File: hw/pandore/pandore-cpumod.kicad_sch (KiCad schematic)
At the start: 11 parts, among them U1 LattePanda_Mu

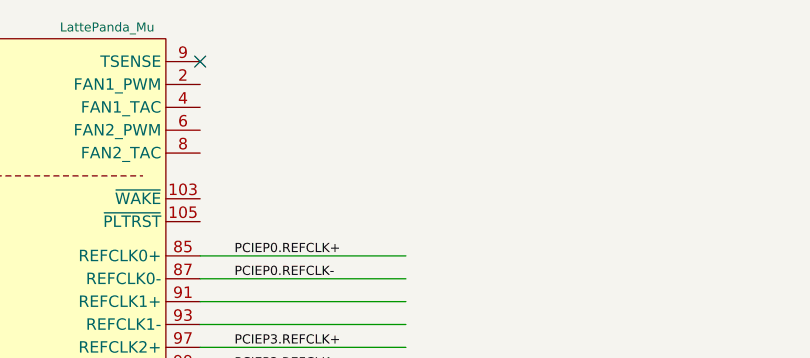
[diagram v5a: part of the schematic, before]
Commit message: lcd control circuit added fan interface added rgba output pinout for management mcu accessories done
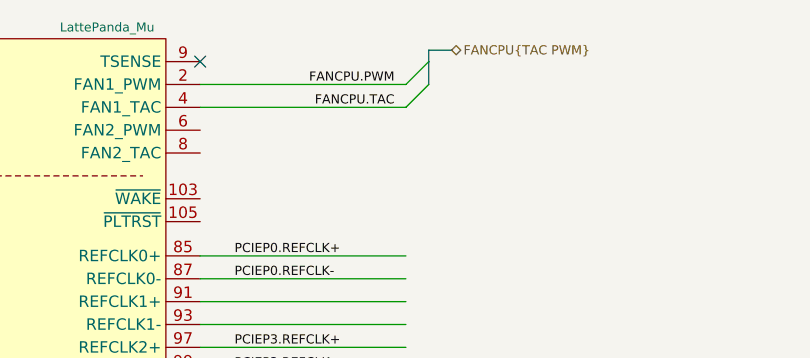
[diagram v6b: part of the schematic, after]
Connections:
- net FANCPU.PWM: now reaches U1.2 (FAN1_PWM)
- net FANCPU.TAC: now reaches U1.4 (FAN1_TAC)
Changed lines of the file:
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@@
 	)
 	(bus_entry
+		(at 246.38 21.59)
+		(size -2.54 2.54)
+		(stroke
+			(width 0)
+			(type default)
+		)
+	)
+	(bus_entry
 		(at 104.14 111.76)
 		(size -2.54 2.54)
@@
 	)
 	(bus_entry
+		(at 246.38 19.05)
+		(size -2.54 2.54)
+		(stroke
+			(width 0)
+			(type default)
+		)
+	)
+	(bus_entry
 		(at 256.54 204.47)
 		(size -2.54 2.54)
@@
 	(wire
 		(pts
+			(xy 220.98 21.59) (xy 243.84 21.59)
+		)
+		(stroke
+			(width 0)
+			(type default)
+		)
+	)
+	(wire
+		(pts
 			(xy 276.86 162.56) (xy 275.59 162.56)
 		)
@@
 		)
 	)
+	(bus
+		(pts
+			(xy 248.92 17.78) (xy 246.38 17.78)
+		)
+		(stroke
+			(width 0)
+			(type default)
+		)
+	)
 	(wire
 		(pts
@@
 	(bus
 		(pts
+			(xy 246.38 19.05) (xy 246.38 21.59)
+		)
+		(stroke
+			(width 0)
+			(type default)
+		)
+	)
+	(bus
+		(pts
 			(xy 104.14 114.3) (xy 104.14 115.57)
 		)
@@
 	(bus
 		(pts
+			(xy 246.38 17.78) (xy 246.38 19.05)
+		)
+		(stroke
+			(width 0)
+			(type default)
+		)
+	)
+	(bus
+		(pts
 			(xy 104.14 95.25) (xy 104.14 97.79)
 		)
@@
 	(wire
 		(pts
+			(xy 220.98 24.13) (xy 243.84 24.13)
+		)
+		(stroke
+			(width 0)
+			(type default)
+		)
+	)
+	(wire
+		(pts
 			(xy 106.68 52.07) (xy 137.16 52.07)
 		)
@@
 		)
 	)
+	(label "FANCPU.TAC"
+		(at 242.57 24.13 180)
+		(effects
+			(font
+				(size 1.016 1.016)
+			)
+			(justify right bottom)
+		)
+	)
 	(label "USBP7.D-"
 		(at 134.62 156.21 180)
@@
 		)
 	)
+	(label "FANCPU.PWM"
+		(at 242.57 21.59 180)
+		(effects
+			(font
+				(size 1.016 1.016)
+			)
+			(justify right bottom)
+		)
+	)
 	(label "USBP3.D-"
 		(at 134.62 146.05 180)
@@
 		)
 	)
+	(hierarchical_label "FANCPU{TAC PWM}"
+		(shape bidirectional)
+		(at 248.92 17.78 0)
+		(effects
+			(font
+				(size 1.016 1.016)
+			)
+			(justify left)
+		)
+	)

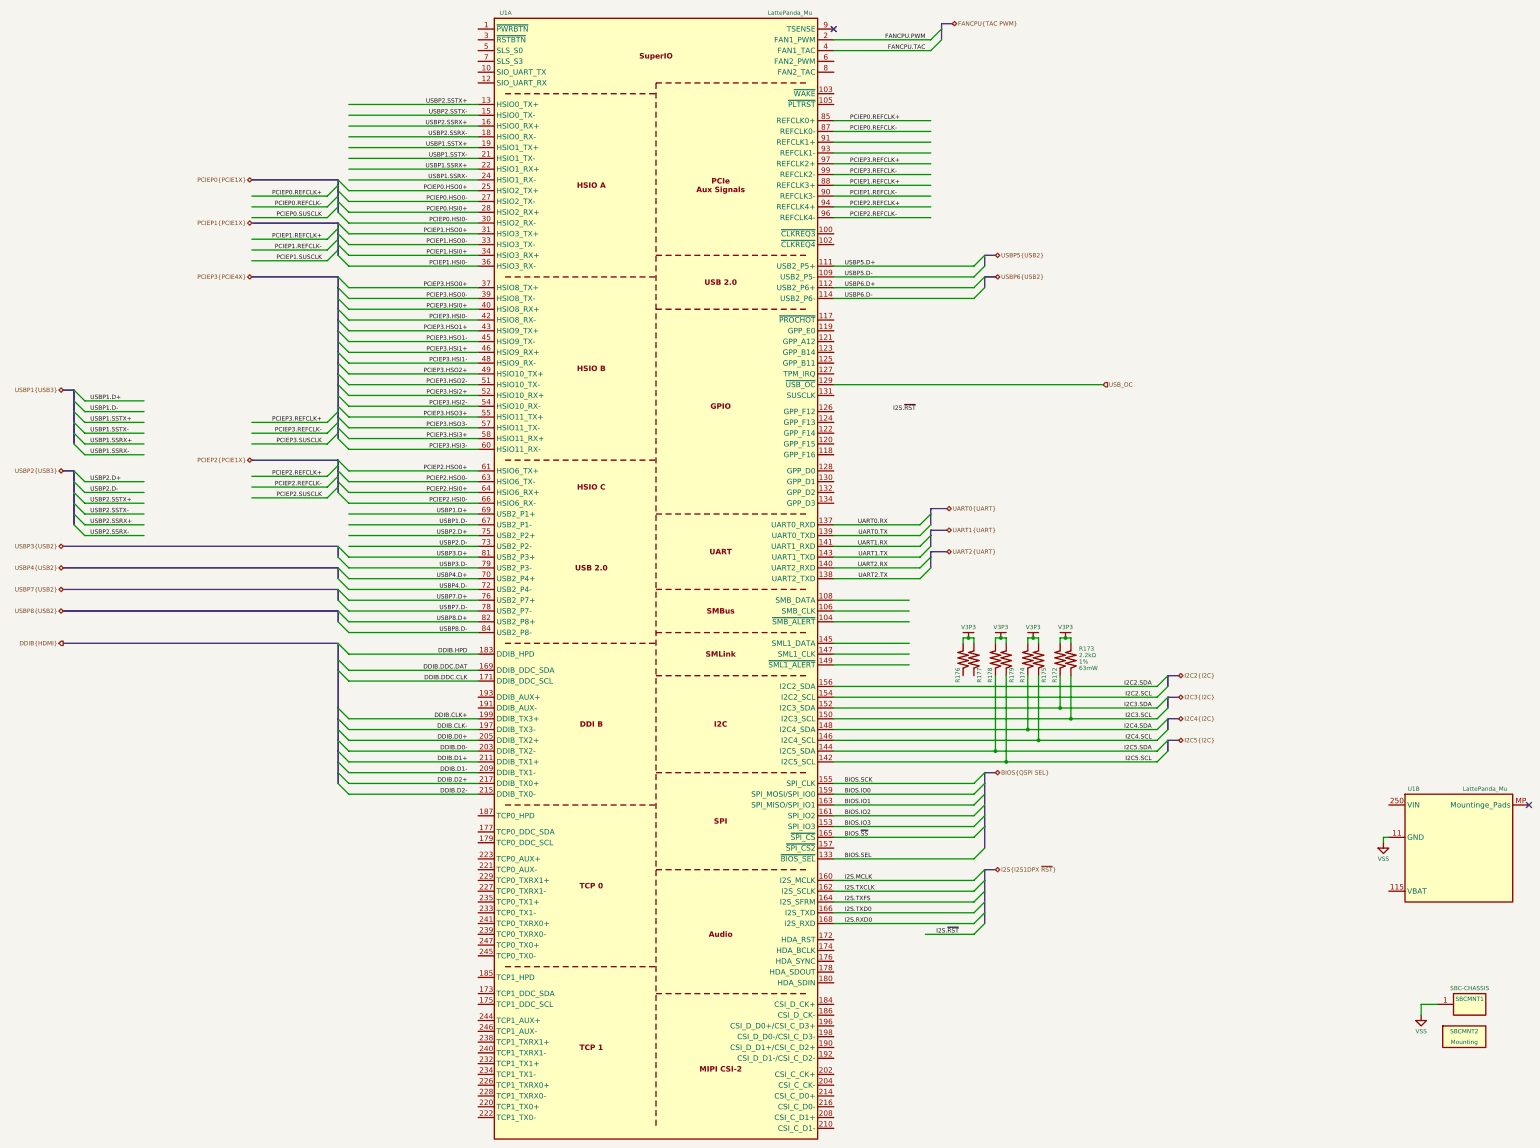
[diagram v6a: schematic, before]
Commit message: most of board control signals added, routed and defined
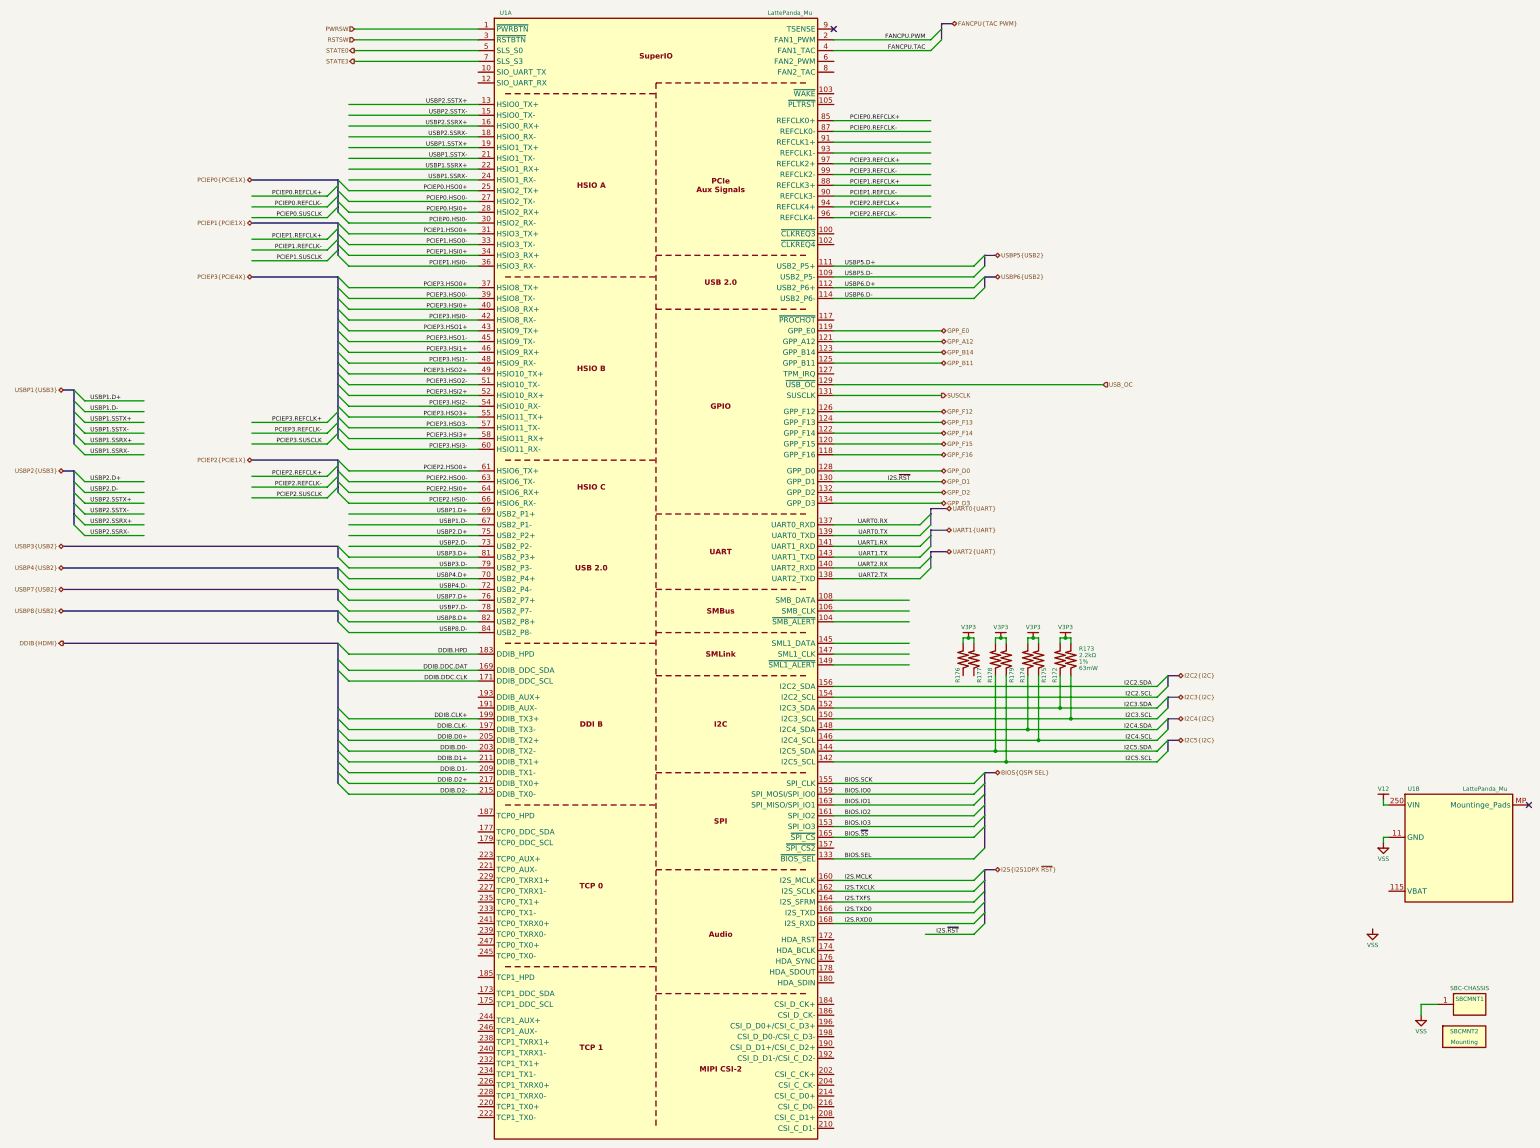
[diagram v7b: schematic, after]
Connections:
- net V12: now reaches U1.250 (VIN), U1.251 (VIN), U1.252 (VIN), U1.253 (VIN), U1.254 (VIN), U1.255 (VIN), U1.256 (VIN), U1.257 (VIN), U1.258 (VIN), U1.259 (VIN), U1.260 (VIN)
- net PWRSW: now reaches U1.1 (~{PWRBTN})
- net GPP_F16: now reaches U1.118 (GPP_F16)
- net GPP_E0: now reaches U1.119 (GPP_E0)
- net GPP_F15: now reaches U1.120 (GPP_F15)
- net GPP_A12: now reaches U1.121 (GPP_A12)
- net GPP_F14: now reaches U1.122 (GPP_F14)
- net GPP_B14: now reaches U1.123 (GPP_B14)
- net GPP_F13: now reaches U1.124 (GPP_F13)
- net GPP_B11: now reaches U1.125 (GPP_B11)
- net GPP_F12: now reaches U1.126 (GPP_F12)
- net GPP_D0: now reaches U1.128 (GPP_D0)
- net GPP_D1: now reaches U1.130 (GPP_D1)
- net SUSCLK: now reaches U1.131 (SUSCLK)
- net GPP_D2: now reaches U1.132 (GPP_D2)
- net GPP_D3: now reaches U1.134 (GPP_D3)
- net RSTSW: now reaches U1.3 (~{RSTBTN})
- net STATE0: now reaches U1.5 (SLS_S0)
- net STATE3: now reaches U1.7 (SLS_S3)

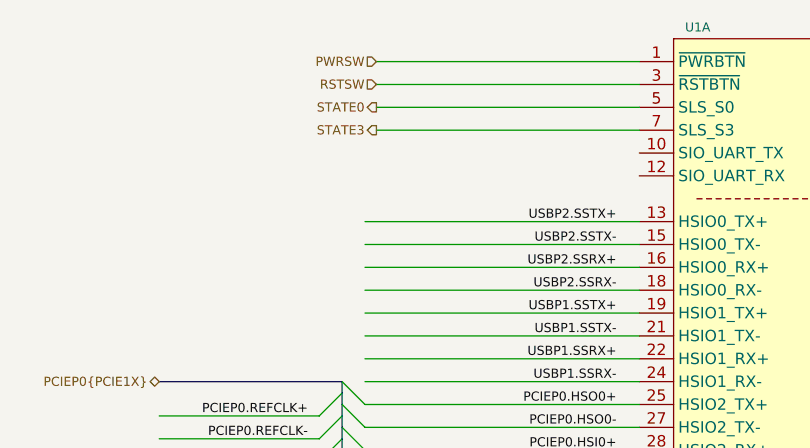
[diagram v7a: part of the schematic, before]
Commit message: added expansion port and more ctl to rp2350s routing much progress
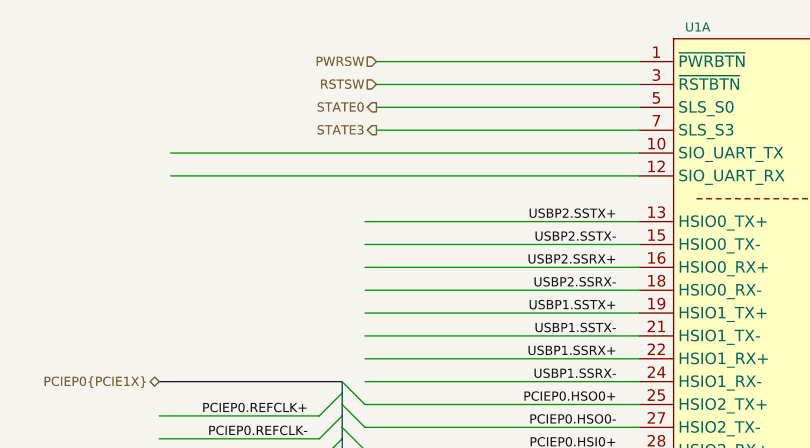
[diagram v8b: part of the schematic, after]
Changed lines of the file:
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@@
+	(wire
+		(pts
+			(xy 85.09 29.21) (xy 137.16 29.21)
+		)
+		(stroke
+			(width 0)
+			(type default)
+		)
+	)
 	(wire
 		(pts
@@
 		)
 		(stroke
+			(width 0)
+			(type default)
+		)
+	)
+	(wire
+		(pts
+			(xy 85.09 31.75) (xy 137.16 31.75)
+		)
+		(stroke
